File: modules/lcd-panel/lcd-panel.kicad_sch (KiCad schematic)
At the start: 9 parts, among them J1 5051100692, J2 5051104091, U1 LP8556SQ-E09/NOPB

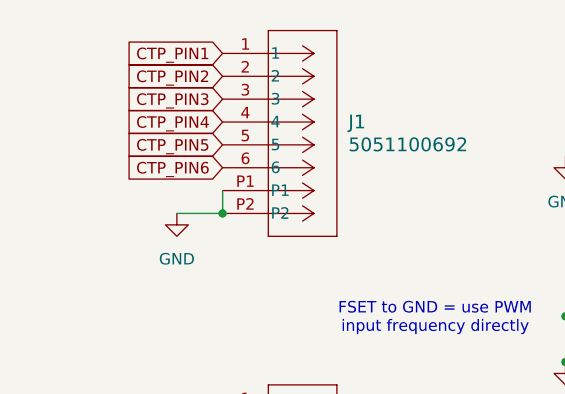
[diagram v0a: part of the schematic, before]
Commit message: update LCD module
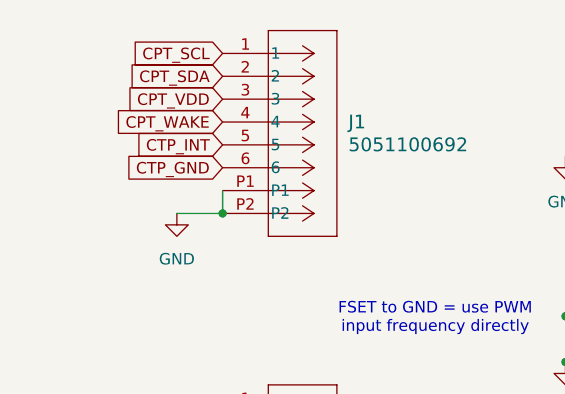
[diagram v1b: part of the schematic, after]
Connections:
- net CTP_PIN1 renamed CPT_SCL
- net CTP_PIN2 renamed CPT_SDA
- net CTP_PIN3 renamed CPT_VDD
- net CTP_PIN4 renamed CPT_WAKE
- net CTP_PIN5 renamed CTP_INT
- net CTP_PIN6 renamed CTP_GND
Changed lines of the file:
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@@
 		)
 	)
-	(global_label "CTP_PIN4"
+	(global_label "CPT_WAKE"
 		(shape input)
 		(at 151.13 31.75 180)
@@
 		)
 		(property "Intersheetrefs" "${INTERSHEET_REFS}"
-			(at 139.2548 31.75 0)
+			(at 138.7106 31.75 0)
 			(effects
 				(font
@@
 		)
 	)
-	(global_label "CTP_PIN2"
+	(global_label "CPT_SDA"
 		(shape input)
 		(at 151.13 26.67 180)
@@
 		)
 		(property "Intersheetrefs" "${INTERSHEET_REFS}"
-			(at 139.2548 26.67 0)
+			(at 140.1015 26.67 0)
 			(effects
 				(font
@@
 		)
 	)
-	(global_label "CTP_PIN6"
+	(global_label "CTP_GND"
 		(shape input)
 		(at 151.13 36.83 180)
@@
 		)
 		(property "Intersheetrefs" "${INTERSHEET_REFS}"
-			(at 139.2548 36.83 0)
+			(at 139.7991 36.83 0)
 			(effects
 				(font
@@
 		)
 	)
-	(global_label "CTP_PIN3"
+	(global_label "CPT_VDD"
 		(shape input)
 		(at 151.13 29.21 180)
@@
 		)
 		(property "Intersheetrefs" "${INTERSHEET_REFS}"
-			(at 139.2548 29.21 0)
+			(at 140.041 29.21 0)
 			(effects
 				(font
@@
 		)
 	)
-	(global_label "CTP_PIN1"
+	(global_label "CPT_SCL"
 		(shape input)
 		(at 151.13 24.13 180)
@@
 		)
 		(property "Intersheetrefs" "${INTERSHEET_REFS}"
-			(at 139.2548 24.13 0)
+			(at 140.162 24.13 0)
 			(effects
 				(font
@@
 		)
 	)
-	(global_label "CTP_PIN5"
+	(global_label "CTP_INT"
 		(shape input)
 		(at 151.13 34.29 180)
@@
 		)
 		(property "Intersheetrefs" "${INTERSHEET_REFS}"
-			(at 139.2548 34.29 0)
-			(effects
-				(font
+			(at 140.7667 34.29 0)
+			(effects
+				(font
